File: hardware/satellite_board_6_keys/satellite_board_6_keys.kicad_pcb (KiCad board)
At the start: 4 copper layers, 60.7 x 52.6 mm, 20 parts, among them J1 Conn_01x02_Socket, J2 Conn_01x06_Socket, J3 Conn_01x06_Socket, J4 Conn_02x12_Odd_Even, J5 Conn_02x12_Odd_Even, U1 CD74HCT251E, U2 CD74HCT251E

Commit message: First routing of the satellite board
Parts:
- moved REF** 51.5 mm to (92.1, 137.2)
- moved REF** 51.5 mm to (144.8, 137.2)
- moved JP5 50.2 mm to (116.8, 123.2)
- moved J5 50.1 mm to (90.8, 101.6)
- moved J4 49.6 mm to (143.5, 101.6)
- moved C1 34.6 mm to (143.0, 79.3)
- moved JP1 32.6 mm to (143.0, 65.3)
- moved JP3 32.0 mm to (116.8, 95.2)
- moved U2 31.6 mm to (132.9, 85.7)
- moved R2 31.3 mm to (129.0, 48.9)
- moved JP4 30.2 mm to (116.8, 102.9)
- moved JP2 22.7 mm to (143.0, 56.6)
- moved C2 20.8 mm to (114.0, 79.8)
- moved U1 17.3 mm to (103.2, 85.7)
- moved R1 16.5 mm to (99.1, 48.9)
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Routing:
- net GND: track 0.00 -> 244.4 mm, vias 0 -> 4
- net VCC: track 0.00 -> 200.1 mm, vias 0 -> 1
- net Net-(J3-Pin_5): track 0.00 -> 112.6 mm
- net Net-(J3-Pin_3): track 0.00 -> 99.8 mm, vias 0 -> 1
- net Net-(J1-Pin_1): track 0.00 -> 84.1 mm, vias 0 -> 1
- net Net-(JP5-Pin_1): track 0.00 -> 83.6 mm, vias 0 -> 1
- net Net-(J3-Pin_1): track 0.00 -> 80.3 mm, vias 0 -> 2
- net Net-(J2-Pin_2): track 0.00 -> 80.2 mm, vias 0 -> 3
- net Net-(J3-Pin_6): track 0.00 -> 73.3 mm, vias 0 -> 1
- net Net-(J4-Pin_3): track 0.00 -> 70.4 mm, vias 0 -> 1
- net Net-(J4-Pin_4): track 0.00 -> 70.1 mm
- net Net-(J4-Pin_5): track 0.00 -> 69.5 mm
- net Net-(J2-Pin_4): track 0.00 -> 69.5 mm, vias 0 -> 3
- net Net-(J2-Pin_1): track 0.00 -> 69.1 mm, vias 0 -> 3
- net Net-(J4-Pin_19): track 0.00 -> 64.3 mm
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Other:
- board size 60.7 x 52.6 mm -> 62 x 103.7 mm
- copper layers 4 -> 2

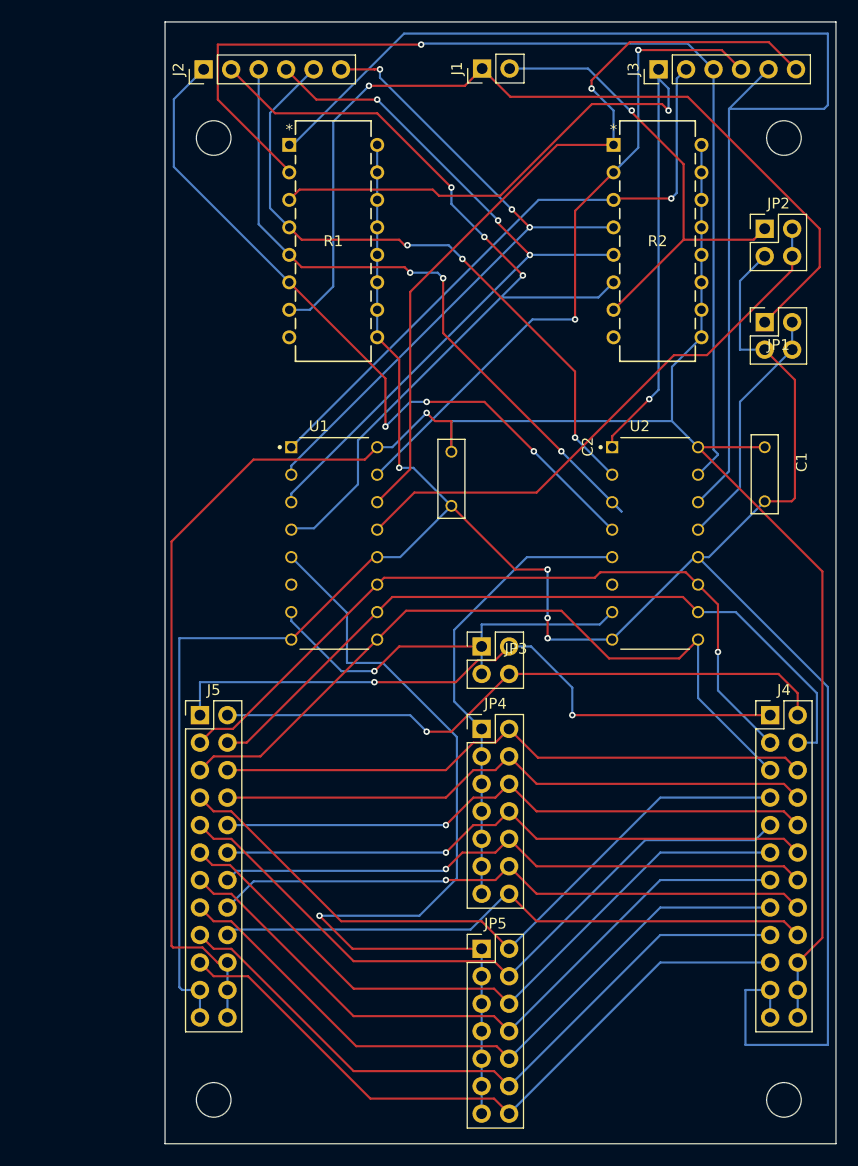
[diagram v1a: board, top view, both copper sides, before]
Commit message: PCB order sent to manufacturer
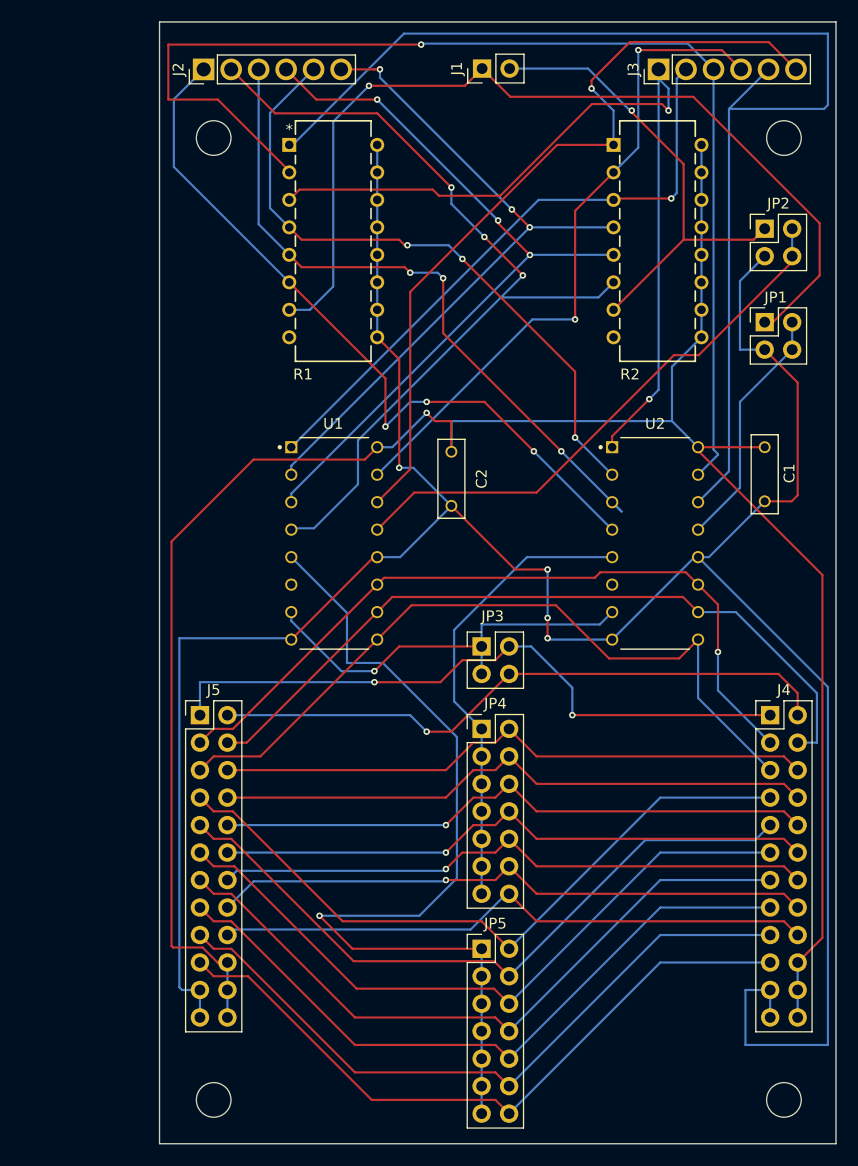
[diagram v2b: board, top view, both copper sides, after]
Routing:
- net Net-(J3-Pin_3): track 99.8 -> 108.9 mm
- net Net-(J1-Pin_1): track 84.1 -> 84.8 mm
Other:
- board size 62 x 103.7 mm -> 62.5 x 103.7 mm
